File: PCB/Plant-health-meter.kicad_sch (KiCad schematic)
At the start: 0 parts

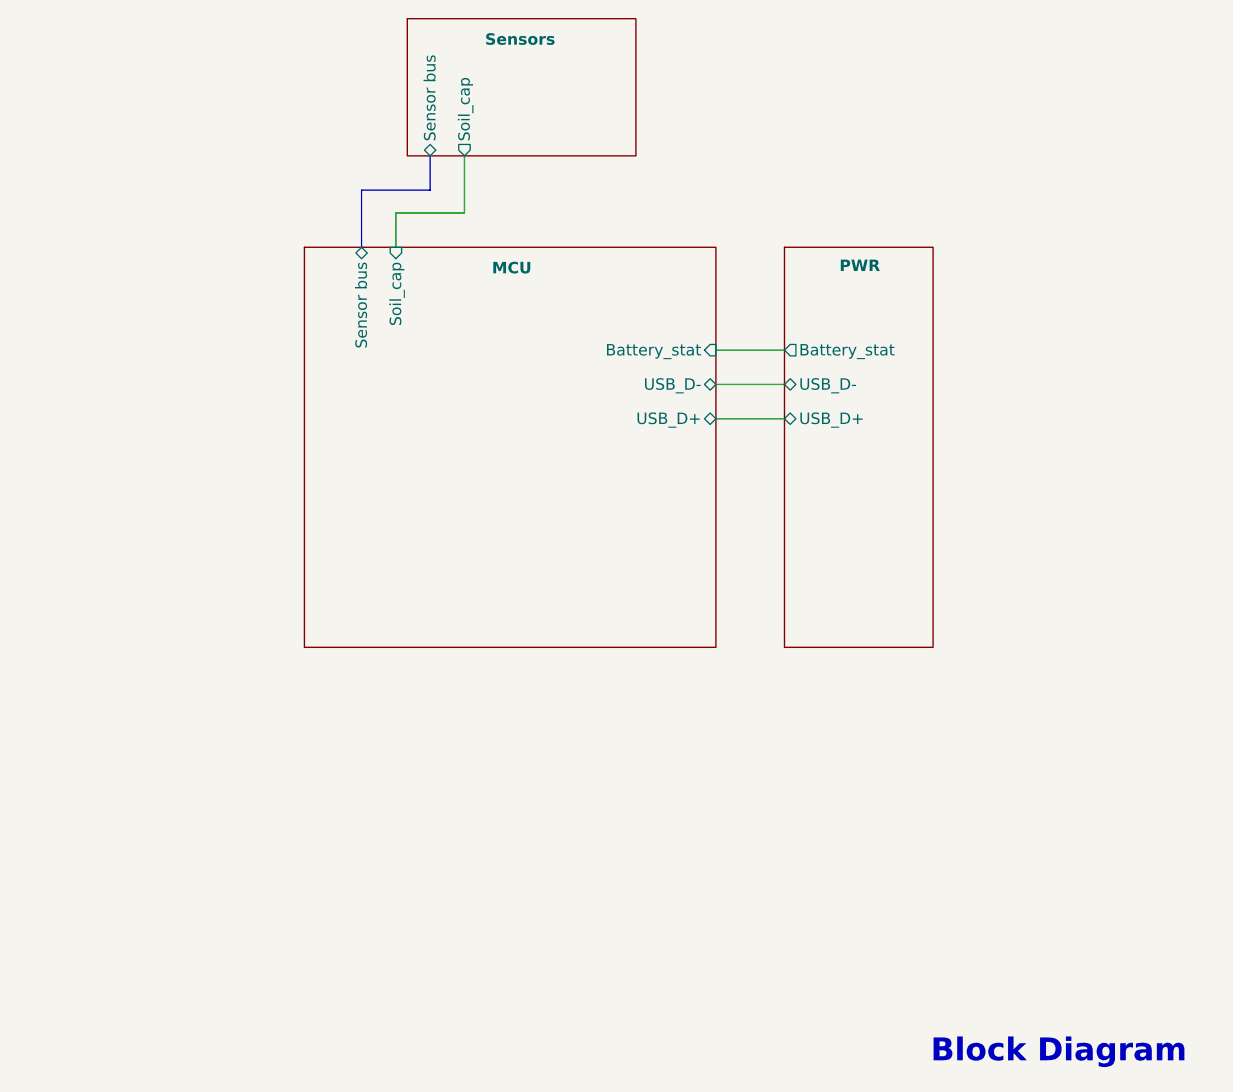
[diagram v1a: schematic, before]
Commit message: Updated some component packages
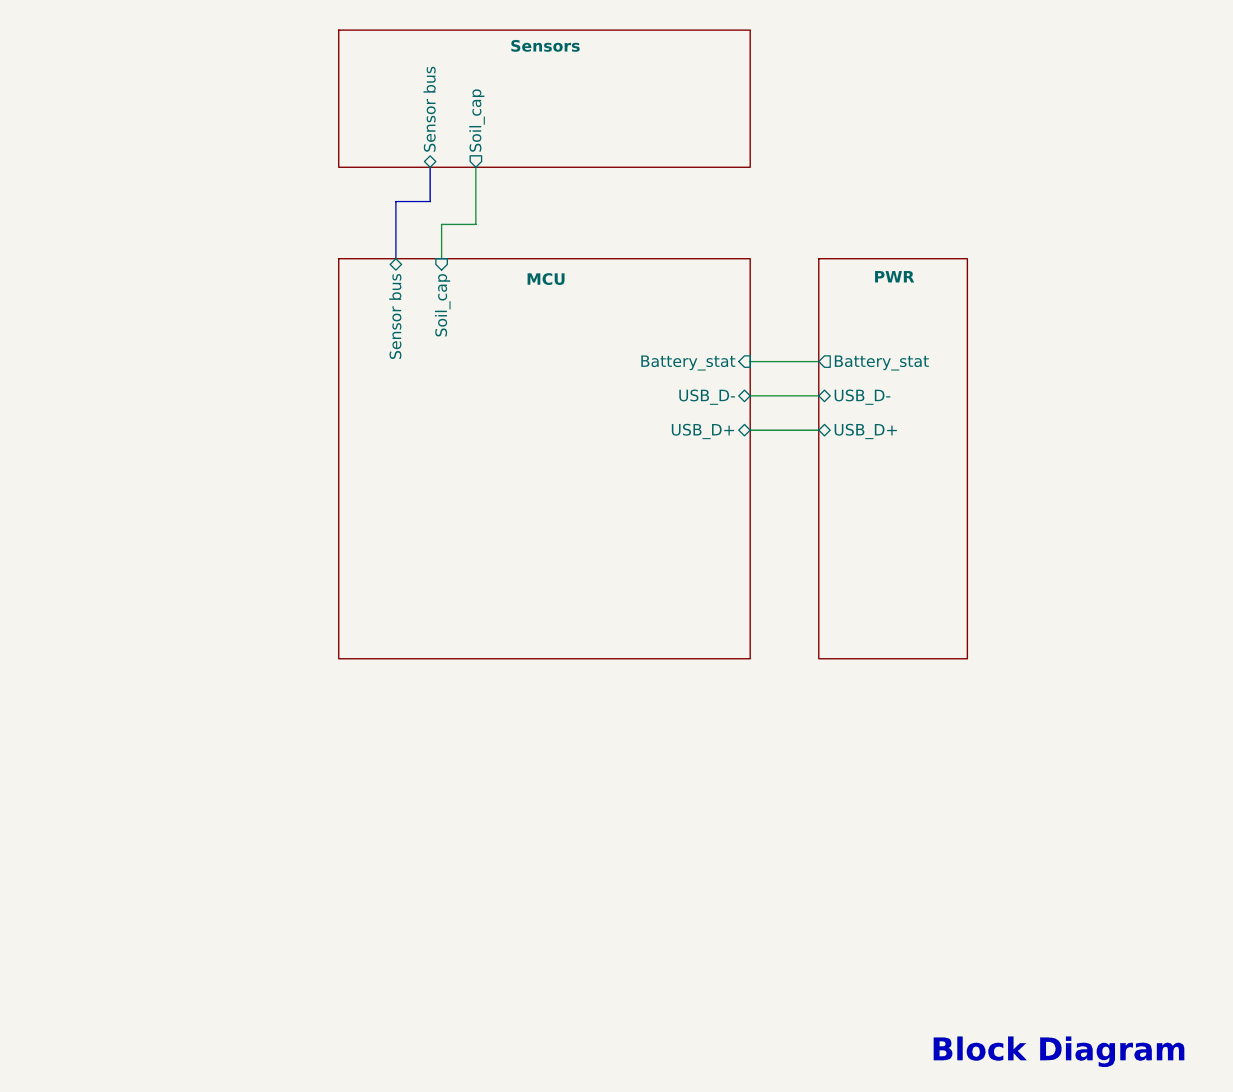
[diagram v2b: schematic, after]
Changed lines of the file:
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@@
 	(wire
 		(pts
-			(xy 129.54 74.93) (xy 129.54 81.28)
+			(xy 130.81 76.2) (xy 130.81 82.55)
 		)
 		(stroke
@@
 	(bus
 		(pts
-			(xy 118.11 78.74) (xy 118.11 85.09)
-		)
-		(stroke
-			(width 0)
-			(type default)
-		)
-	)
-	(wire
-		(pts
-			(xy 129.54 81.28) (xy 121.92 81.28)
-		)
-		(stroke
-			(width 0)
-			(type default)
-		)
-	)
-	(wire
-		(pts
-			(xy 157.48 96.52) (xy 165.1 96.52)
+			(xy 121.92 80.01) (xy 121.92 86.36)
+		)
+		(stroke
+			(width 0)
+			(type default)
+		)
+	)
+	(wire
+		(pts
+			(xy 130.81 82.55) (xy 127 82.55)
+		)
+		(stroke
+			(width 0)
+			(type default)
+		)
+	)
+	(wire
+		(pts
+			(xy 161.29 97.79) (xy 168.91 97.79)
 		)
 		(stroke
@@
 	(bus
 		(pts
-			(xy 125.73 74.93) (xy 125.73 78.74)
-		)
-		(stroke
-			(width 0)
-			(type default)
-		)
-	)
-	(wire
-		(pts
-			(xy 157.48 104.14) (xy 165.1 104.14)
+			(xy 125.73 76.2) (xy 125.73 80.01)
+		)
+		(stroke
+			(width 0)
+			(type default)
+		)
+	)
+	(wire
+		(pts
+			(xy 161.29 105.41) (xy 168.91 105.41)
 		)
 		(stroke
@@
 	(bus
 		(pts
-			(xy 125.73 78.74) (xy 118.11 78.74)
-		)
-		(stroke
-			(width 0)
-			(type default)
-		)
-	)
-	(wire
-		(pts
-			(xy 157.48 100.33) (xy 165.1 100.33)
-		)
-		(stroke
-			(width 0)
-			(type default)
-		)
-	)
-	(wire
-		(pts
-			(xy 121.92 81.28) (xy 121.92 85.09)
+			(xy 125.73 80.01) (xy 121.92 80.01)
+		)
+		(stroke
+			(width 0)
+			(type default)
+		)
+	)
+	(wire
+		(pts
+			(xy 161.29 101.6) (xy 168.91 101.6)
+		)
+		(stroke
+			(width 0)
+			(type default)
+		)
+	)
+	(wire
+		(pts
+			(xy 127 82.55) (xy 127 86.36)
 		)
 		(stroke
@@
 	)
 	(sheet
-		(at 123.19 59.69)
-		(size 25.4 15.24)
+		(at 115.57 60.96)
+		(size 45.72 15.24)
 		(stroke
 			(width 0.1524)
@@
 		)
 		(property "Sheetname" "Sensors"
-			(at 131.826 62.738 0)
+			(at 134.62 63.5 0)
 			(effects
 				(font
@@
 		)
 		(property "Sheetfile" "sensors.kicad_sch"
-			(at 123.19 78.0546 0)
+			(at 115.57 79.3246 0)
 			(effects
 				(font
@@
 		)
 		(pin "Sensor bus" bidirectional
-			(at 125.73 74.93 270)
+			(at 125.73 76.2 270)
 			(effects
 				(font
@@
 		)
 		(pin "Soil_cap" output
-			(at 129.54 74.93 270)
+			(at 130.81 76.2 270)
 			(effects
 				(font
@@
 	)
 	(sheet
-		(at 165.1 85.09)
+		(at 168.91 86.36)
 		(size 16.51 44.45)
 		(stroke
@@
 		)
 		(property "Sheetname" "PWR"
-			(at 171.196 87.884 0)
+			(at 175.006 89.154 0)
 			(effects
 				(font
@@
 		)
 		(property "Sheetfile" "pwr.kicad_sch"
-			(at 165.1 158.0646 0)
+			(at 168.91 159.3346 0)
 			(effects
 				(font
@@
 		)
 		(pin "Battery_stat" output
-			(at 165.1 96.52 180)
+			(at 168.91 97.79 180)
 			(effects
 				(font
@@
 		)
 		(pin "USB_D+" bidirectional
-			(at 165.1 104.14 180)
+			(at 168.91 105.41 180)
 			(effects
 				(font
@@
 		)
 		(pin "USB_D-" bidirectional
-			(at 165.1 100.33 180)
+			(at 168.91 101.6 180)
 			(effects
 				(font
@@
 	)
 	(sheet
-		(at 111.76 85.09)
+		(at 115.57 86.36)
 		(size 45.72 44.45)
 		(stroke
@@
 		)
 		(property "Sheetname" "MCU"
-			(at 132.588 88.138 0)
+			(at 136.398 89.408 0)
 			(effects
 				(font
@@
 		)
 		(property "Sheetfile" "mcu.kicad_sch"
-			(at 111.76 130.1246 0)
+			(at 115.57 131.3946 0)
 			(effects
 				(font
@@
 		)
 		(pin "Sensor bus" bidirectional
-			(at 118.11 85.09 90)
+			(at 121.92 86.36 90)
 			(effects
 				(font
@@
 		)
 		(pin "Battery_stat" input
-			(at 157.48 96.52 0)
+			(at 161.29 97.79 0)
 			(effects
 				(font
@@
 		)
 		(pin "USB_D-" bidirectional
-			(at 157.48 100.33 0)
+			(at 161.29 101.6 0)
 			(effects
 				(font
@@
 		)
 		(pin "USB_D+" bidirectional
-			(at 157.48 104.14 0)
+			(at 161.29 105.41 0)
 			(effects
 				(font
@@
 		)
 		(pin "Soil_cap" input
-			(at 121.92 85.09 90)
-			(effects
-				(font
+			(at 127 86.36 90)
+			(effects
+				(font

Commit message: Added light sensor simulation and schematic
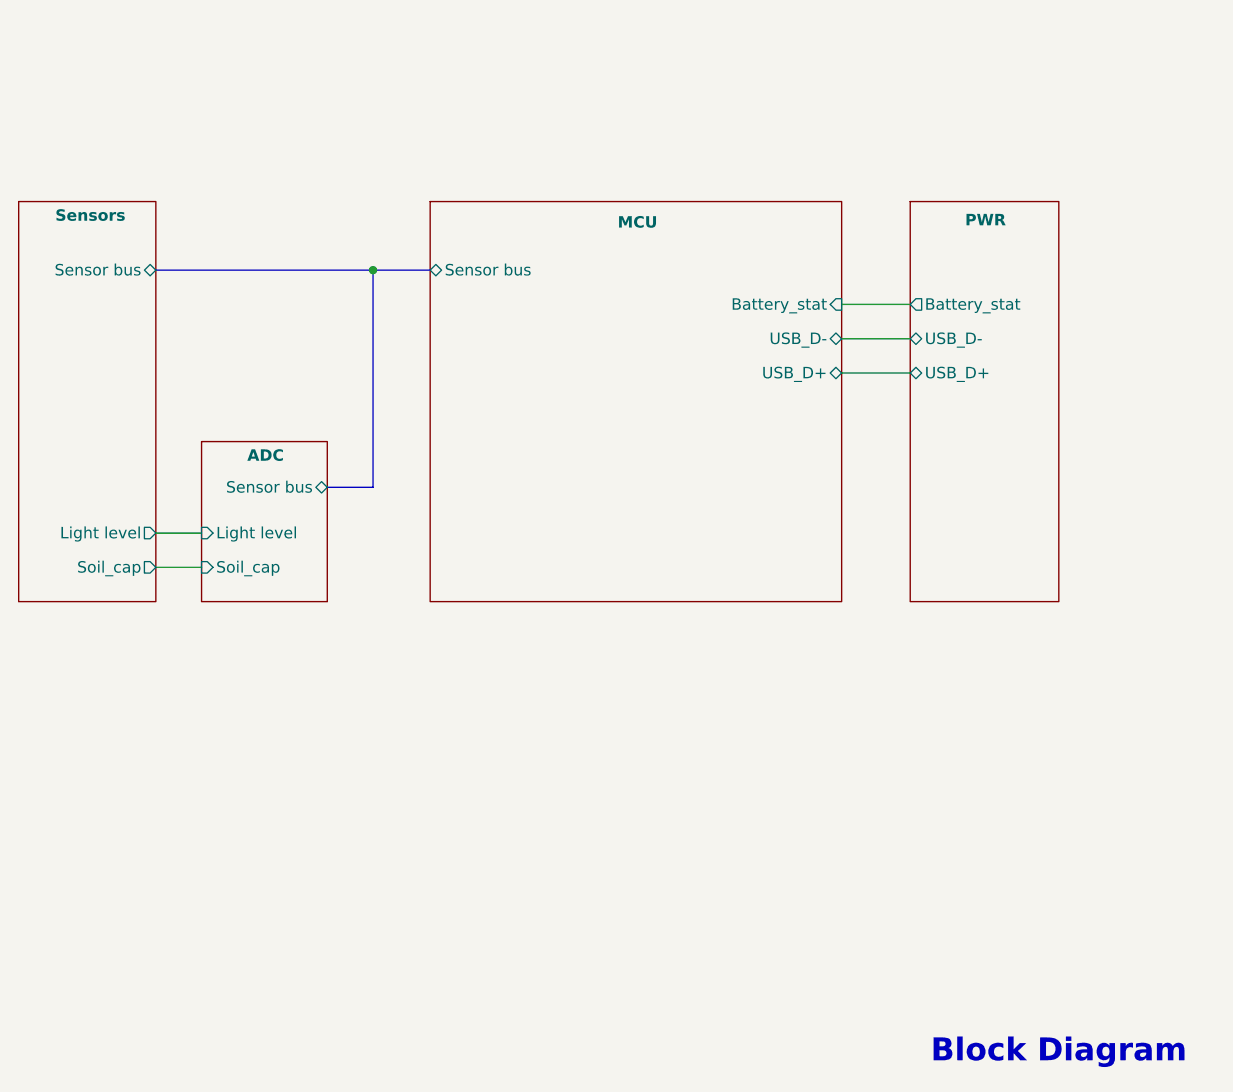
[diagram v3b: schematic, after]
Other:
- added sheet ADC (adc.kicad_sch)
- sheet MCU ports: added none; removed Soil_cap
- sheet Sensors ports: added Light level; removed none
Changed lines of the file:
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@@
 	(generator_version "8.0")
 	(paper "A4")
-	(wire
-		(pts
-			(xy 130.81 76.2) (xy 130.81 82.55)
-		)
-		(stroke
-			(width 0)
-			(type default)
-		)
+	(junction
+		(at 119.38 87.63)
+		(diameter 0)
+		(color 0 0 0 0)
 	)
 	(bus
 		(pts
-			(xy 121.92 80.01) (xy 121.92 86.36)
-		)
-		(stroke
-			(width 0)
-			(type default)
-		)
-	)
-	(wire
-		(pts
-			(xy 130.81 82.55) (xy 127 82.55)
-		)
-		(stroke
-			(width 0)
-			(type default)
-		)
-	)
-	(wire
-		(pts
-			(xy 161.29 97.79) (xy 168.91 97.79)
+			(xy 114.3 111.76) (xy 119.38 111.76)
+		)
+		(stroke
+			(width 0)
+			(type default)
+		)
+	)
+	(wire
+		(pts
+			(xy 95.25 120.65) (xy 100.33 120.65)
+		)
+		(stroke
+			(width 0)
+			(type default)
+		)
+	)
+	(wire
+		(pts
+			(xy 171.45 91.44) (xy 179.07 91.44)
 		)
 		(stroke
@@
 	(bus
 		(pts
-			(xy 125.73 76.2) (xy 125.73 80.01)
-		)
-		(stroke
-			(width 0)
-			(type default)
-		)
-	)
-	(wire
-		(pts
-			(xy 161.29 105.41) (xy 168.91 105.41)
+			(xy 119.38 87.63) (xy 125.73 87.63)
 		)
 		(stroke
@@
 	(bus
 		(pts
-			(xy 125.73 80.01) (xy 121.92 80.01)
-		)
-		(stroke
-			(width 0)
-			(type default)
-		)
-	)
-	(wire
-		(pts
-			(xy 161.29 101.6) (xy 168.91 101.6)
-		)
-		(stroke
-			(width 0)
-			(type default)
-		)
-	)
-	(wire
-		(pts
-			(xy 127 82.55) (xy 127 86.36)
+			(xy 95.25 87.63) (xy 119.38 87.63)
+		)
+		(stroke
+			(width 0)
+			(type default)
+		)
+	)
+	(wire
+		(pts
+			(xy 95.25 116.84) (xy 100.33 116.84)
+		)
+		(stroke
+			(width 0)
+			(type default)
+		)
+	)
+	(wire
+		(pts
+			(xy 171.45 99.06) (xy 179.07 99.06)
+		)
+		(stroke
+			(width 0)
+			(type default)
+		)
+	)
+	(bus
+		(pts
+			(xy 119.38 111.76) (xy 119.38 87.63)
+		)
+		(stroke
+			(width 0)
+			(type default)
+		)
+	)
+	(wire
+		(pts
+			(xy 171.45 95.25) (xy 179.07 95.25)
 		)
 		(stroke
@@
 	)
 	(sheet
-		(at 115.57 60.96)
-		(size 45.72 15.24)
+		(at 100.33 106.68)
+		(size 13.97 17.78)
 		(stroke
 			(width 0.1524)
@@
 			(color 200 200 200 1.0000)
 		)
-		(property "Sheetname" "Sensors"
-			(at 134.62 63.5 0)
+		(property "Sheetname" "ADC"
+			(at 105.41 108.966 0)
 			(effects
 				(font
@@
 			)
 		)
-		(property "Sheetfile" "sensors.kicad_sch"
-			(at 115.57 79.3246 0)
+		(property "Sheetfile" "adc.kicad_sch"
+			(at 100.33 126.3146 0)
 			(effects
 				(font
@@
 			)
 		)
+		(pin "Soil_cap" input
+			(at 100.33 120.65 180)
+			(effects
+				(font
+					(size 1.27 1.27)
+				)
+				(justify left)
+			)
+		)
 		(pin "Sensor bus" bidirectional
-			(at 125.73 76.2 270)
-			(effects
-				(font
-					(size 1.27 1.27)
-				)
-				(justify left)
-			)
-		)
-		(pin "Soil_cap" output
-			(at 130.81 76.2 270)
+			(at 114.3 111.76 0)
+			(effects
+				(font
+					(size 1.27 1.27)
+				)
+				(justify right)
+			)
+		)
+		(pin "Light level" input
+			(at 100.33 116.84 180)
 			(effects
 				(font
@@
 	)
 	(sheet
-		(at 168.91 86.36)
-		(size 16.51 44.45)
+		(at 80.01 80.01)
+		(size 15.24 44.45)
 		(stroke
 			(width 0.1524)
@@
 			(color 200 200 200 1.0000)
 		)
-		(property "Sheetname" "PWR"
-			(at 175.006 89.154 0)
+		(property "Sheetname" "Sensors"
+			(at 84.074 82.296 0)
 			(effects
 				(font
@@
 			)
 		)
-		(property "Sheetfile" "pwr.kicad_sch"
-			(at 168.91 159.3346 0)
+		(property "Sheetfile" "sensors.kicad_sch"
+			(at 80.01 98.3746 0)
 			(effects
 				(font
@@
 			)
 		)
+		(pin "Sensor bus" bidirectional
+			(at 95.25 87.63 0)
+			(effects
+				(font
+					(size 1.27 1.27)
+				)
+				(justify right)
+			)
+		)
+		(pin "Soil_cap" output
+			(at 95.25 120.65 0)
+			(effects
+				(font
+					(size 1.27 1.27)
+				)
+				(justify right)
+			)
+		)
+		(pin "Light level" output
+			(at 95.25 116.84 0)
+			(effects
+				(font
+					(size 1.27 1.27)
+				)
+				(justify right)
+			)
+		)
+		(instances
+			(project "Plant-health-meter"
+				(path "/357055bf-c309-4d6b-a2fa-f5ee5ba59771"
+					(page "5")
+				)
+			)
+		)
+	)
+	(sheet
+		(at 179.07 80.01)
+		(size 16.51 44.45)
+		(stroke
+			(width 0.1524)
+			(type solid)
+			(color 0 0 0 1)
+		)
+		(fill
+			(color 200 200 200 1.0000)
+		)
+		(property "Sheetname" "PWR"
+			(at 185.166 82.804 0)
+			(effects
+				(font
+					(size 1.27 1.27)
+					(thickness 0.254)
+					(bold yes)
+				)
+				(justify left bottom)
+			)
+		)
+		(property "Sheetfile" "pwr.kicad_sch"
+			(at 179.07 152.9846 0)
+			(effects
+				(font
+					(size 1.27 1.27)
+				)
+				(justify left top)
+				(hide yes)
+			)
+		)
 		(pin "Battery_stat" output
-			(at 168.91 97.79 180)
+			(at 179.07 91.44 180)
 			(effects
 				(font
@@
 		)
 		(pin "USB_D+" bidirectional
-			(at 168.91 105.41 180)
+			(at 179.07 99.06 180)
 			(effects
 				(font
@@
 		)
 		(pin "USB_D-" bidirectional
-			(at 168.91 101.6 180)
+			(at 179.07 95.25 180)
 			(effects
 				(font
@@
 	)
 	(sheet
-		(at 115.57 86.36)
+		(at 125.73 80.01)
 		(size 45.72 44.45)
 		(stroke
@@
 		)
 		(property "Sheetname" "MCU"
-			(at 136.398 89.408 0)
+			(at 146.558 83.058 0)
 			(effects
 				(font
@@
 		)
 		(property "Sheetfile" "mcu.kicad_sch"
-			(at 115.57 131.3946 0)
+			(at 125.73 125.0446 0)
 			(effects
 				(font
@@
 		)
 		(pin "Sensor bus" bidirectional
-			(at 121.92 86.36 90)
-			(effects
-				(font
-					(size 1.27 1.27)
-				)
-				(justify right)
+			(at 125.73 87.63 180)
+			(effects
+				(font
+					(size 1.27 1.27)
+				)
+				(justify left)
 			)
 		)
 		(pin "Battery_stat" input
-			(at 161.29 97.79 0)
+			(at 171.45 91.44 0)
 			(effects
 				(font
@@
 		)
 		(pin "USB_D-" bidirectional
-			(at 161.29 101.6 0)
+			(at 171.45 95.25 0)
 			(effects
 				(font
@@
 		)
 		(pin "USB_D+" bidirectional
-			(at 161.29 105.41 0)
-			(effects
-				(font
-					(size 1.27 1.27)
-				)
-				(justify right)
-			)
-		)
-		(pin "Soil_cap" input
-			(at 127 86.36 90)
-			(effects
-				(font
+			(at 171.45 99.06 0)
+			(effects
+				(font

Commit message: Light sensor
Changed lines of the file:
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@@
 	(paper "A4")
 	(junction
-		(at 119.38 87.63)
+		(at 132.08 85.09)
 		(diameter 0)
 		(color 0 0 0 0)
@@
 	(bus
 		(pts
-			(xy 114.3 111.76) (xy 119.38 111.76)
-		)
-		(stroke
-			(width 0)
-			(type default)
-		)
-	)
-	(wire
-		(pts
-			(xy 95.25 120.65) (xy 100.33 120.65)
-		)
-		(stroke
-			(width 0)
-			(type default)
-		)
-	)
-	(wire
-		(pts
-			(xy 171.45 91.44) (xy 179.07 91.44)
+			(xy 127 109.22) (xy 132.08 109.22)
+		)
+		(stroke
+			(width 0)
+			(type default)
+		)
+	)
+	(wire
+		(pts
+			(xy 107.95 118.11) (xy 113.03 118.11)
+		)
+		(stroke
+			(width 0)
+			(type default)
+		)
+	)
+	(wire
+		(pts
+			(xy 184.15 88.9) (xy 191.77 88.9)
 		)
 		(stroke
@@
 	(bus
 		(pts
-			(xy 119.38 87.63) (xy 125.73 87.63)
+			(xy 132.08 85.09) (xy 138.43 85.09)
 		)
 		(stroke
@@
 	(bus
 		(pts
-			(xy 95.25 87.63) (xy 119.38 87.63)
-		)
-		(stroke
-			(width 0)
-			(type default)
-		)
-	)
-	(wire
-		(pts
-			(xy 95.25 116.84) (xy 100.33 116.84)
-		)
-		(stroke
-			(width 0)
-			(type default)
-		)
-	)
-	(wire
-		(pts
-			(xy 171.45 99.06) (xy 179.07 99.06)
+			(xy 107.95 85.09) (xy 132.08 85.09)
+		)
+		(stroke
+			(width 0)
+			(type default)
+		)
+	)
+	(wire
+		(pts
+			(xy 107.95 114.3) (xy 113.03 114.3)
+		)
+		(stroke
+			(width 0)
+			(type default)
+		)
+	)
+	(wire
+		(pts
+			(xy 184.15 96.52) (xy 191.77 96.52)
 		)
 		(stroke
@@
 	(bus
 		(pts
-			(xy 119.38 111.76) (xy 119.38 87.63)
-		)
-		(stroke
-			(width 0)
-			(type default)
-		)
-	)
-	(wire
-		(pts
-			(xy 171.45 95.25) (xy 179.07 95.25)
+			(xy 132.08 109.22) (xy 132.08 85.09)
+		)
+		(stroke
+			(width 0)
+			(type default)
+		)
+	)
+	(wire
+		(pts
+			(xy 184.15 92.71) (xy 191.77 92.71)
 		)
 		(stroke
@@
 	)
 	(sheet
-		(at 100.33 106.68)
+		(at 113.03 104.14)
 		(size 13.97 17.78)
 		(stroke
@@
 		)
 		(property "Sheetname" "ADC"
-			(at 105.41 108.966 0)
+			(at 118.11 106.426 0)
 			(effects
 				(font
@@
 		)
 		(property "Sheetfile" "adc.kicad_sch"
-			(at 100.33 126.3146 0)
+			(at 113.03 123.7746 0)
 			(effects
 				(font
@@
 		)
 		(pin "Soil_cap" input
-			(at 100.33 120.65 180)
+			(at 113.03 118.11 180)
 			(effects
 				(font
@@
 		)
 		(pin "Sensor bus" bidirectional
-			(at 114.3 111.76 0)
+			(at 127 109.22 0)
 			(effects
 				(font
@@
 		)
 		(pin "Light level" input
-			(at 100.33 116.84 180)
+			(at 113.03 114.3 180)
 			(effects
 				(font
@@
 	)
 	(sheet
-		(at 80.01 80.01)
+		(at 92.71 77.47)
 		(size 15.24 44.45)
 		(stroke
@@
 		)
 		(property "Sheetname" "Sensors"
-			(at 84.074 82.296 0)
+			(at 96.774 79.756 0)
 			(effects
 				(font
@@
 		)
 		(property "Sheetfile" "sensors.kicad_sch"
-			(at 80.01 98.3746 0)
+			(at 92.71 95.8346 0)
 			(effects
 				(font
@@
 		)
 		(pin "Sensor bus" bidirectional
-			(at 95.25 87.63 0)
+			(at 107.95 85.09 0)
 			(effects
 				(font
@@
 		)
 		(pin "Soil_cap" output
-			(at 95.25 120.65 0)
+			(at 107.95 118.11 0)
 			(effects
 				(font
@@
 		)
 		(pin "Light level" output
-			(at 95.25 116.84 0)
+			(at 107.95 114.3 0)
 			(effects
 				(font
@@
 	)
 	(sheet
-		(at 179.07 80.01)
+		(at 191.77 77.47)
 		(size 16.51 44.45)
 		(stroke
@@
 		)
 		(property "Sheetname" "PWR"
-			(at 185.166 82.804 0)
+			(at 197.866 80.264 0)
 			(effects
 				(font
@@
 		)
 		(property "Sheetfile" "pwr.kicad_sch"
-			(at 179.07 152.9846 0)
+			(at 191.77 150.4446 0)
 			(effects
 				(font
@@
 		)
 		(pin "Battery_stat" output
-			(at 179.07 91.44 180)
+			(at 191.77 88.9 180)
 			(effects
 				(font
@@
 		)
 		(pin "USB_D+" bidirectional
-			(at 179.07 99.06 180)
+			(at 191.77 96.52 180)
 			(effects
 				(font
@@
 		)
 		(pin "USB_D-" bidirectional
-			(at 179.07 95.25 180)
+			(at 191.77 92.71 180)
 			(effects
 				(font
@@
 	)
 	(sheet
-		(at 125.73 80.01)
+		(at 138.43 77.47)
 		(size 45.72 44.45)
 		(stroke
@@
 		)
 		(property "Sheetname" "MCU"
-			(at 146.558 83.058 0)
+			(at 159.258 80.518 0)
 			(effects
 				(font
@@
 		)
 		(property "Sheetfile" "mcu.kicad_sch"
-			(at 125.73 125.0446 0)
+			(at 138.43 122.5046 0)
 			(effects
 				(font
@@
 		)
 		(pin "Sensor bus" bidirectional
-			(at 125.73 87.63 180)
+			(at 138.43 85.09 180)
 			(effects
 				(font
@@
 		)
 		(pin "Battery_stat" input
-			(at 171.45 91.44 0)
+			(at 184.15 88.9 0)
 			(effects
 				(font
@@
 		)
 		(pin "USB_D-" bidirectional
-			(at 171.45 95.25 0)
+			(at 184.15 92.71 0)
 			(effects
 				(font
@@
 		)
 		(pin "USB_D+" bidirectional
-			(at 171.45 99.06 0)
-			(effects
-				(font
+			(at 184.15 96.52 0)
+			(effects
+				(font
